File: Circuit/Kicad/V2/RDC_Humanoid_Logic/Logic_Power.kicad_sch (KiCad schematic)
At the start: 5 parts

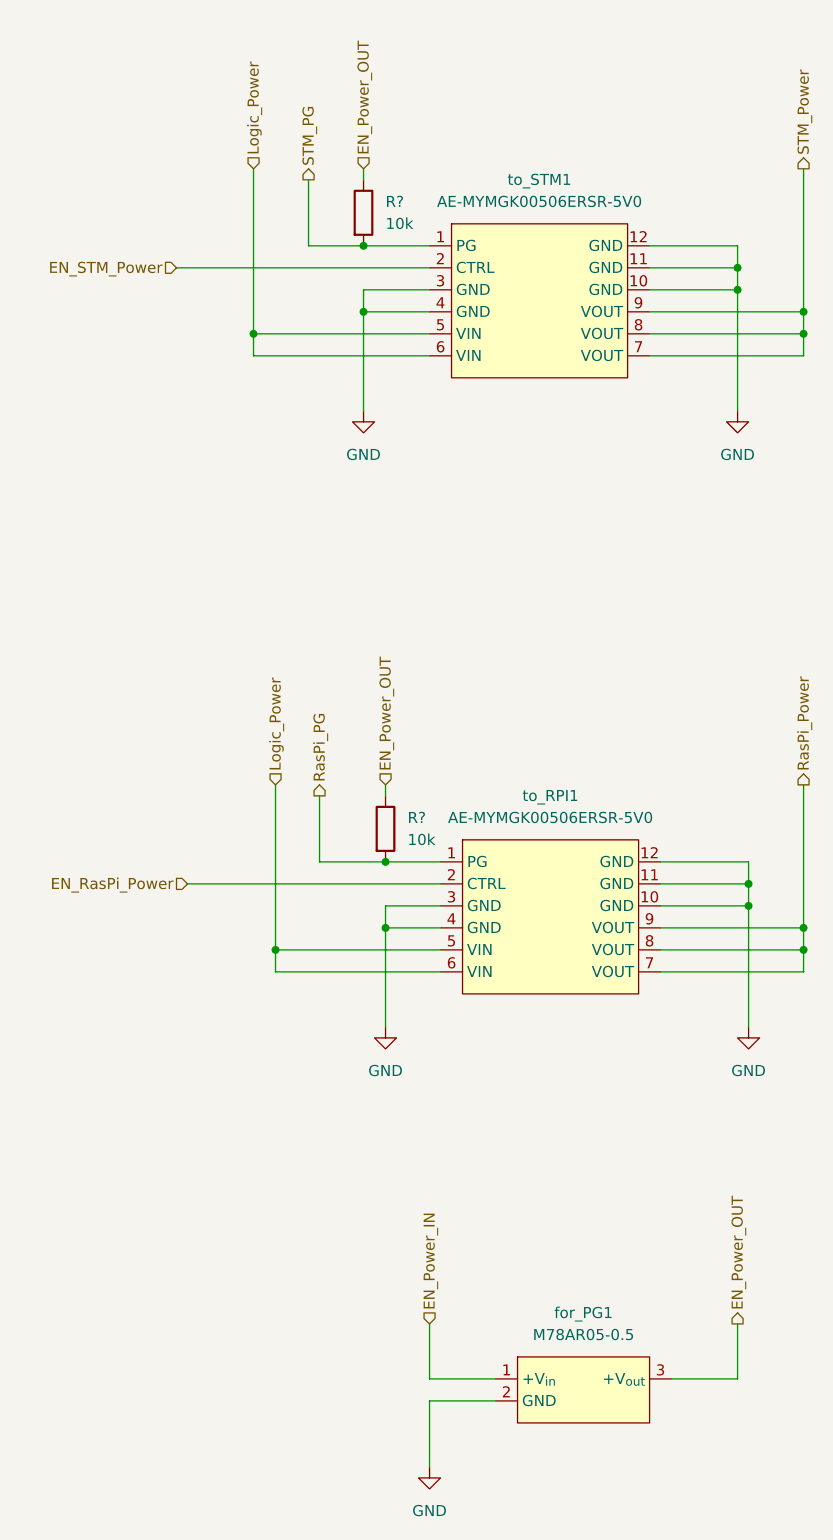
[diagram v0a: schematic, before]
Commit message: V2をUpdate。FrontをベタGND、CANトランシーバのSTANDBYとINをGNDに接続、ビアを複数配置、XT30->XT60に更新、D1を回路図通りショットキーバリアダイオードに変更した。
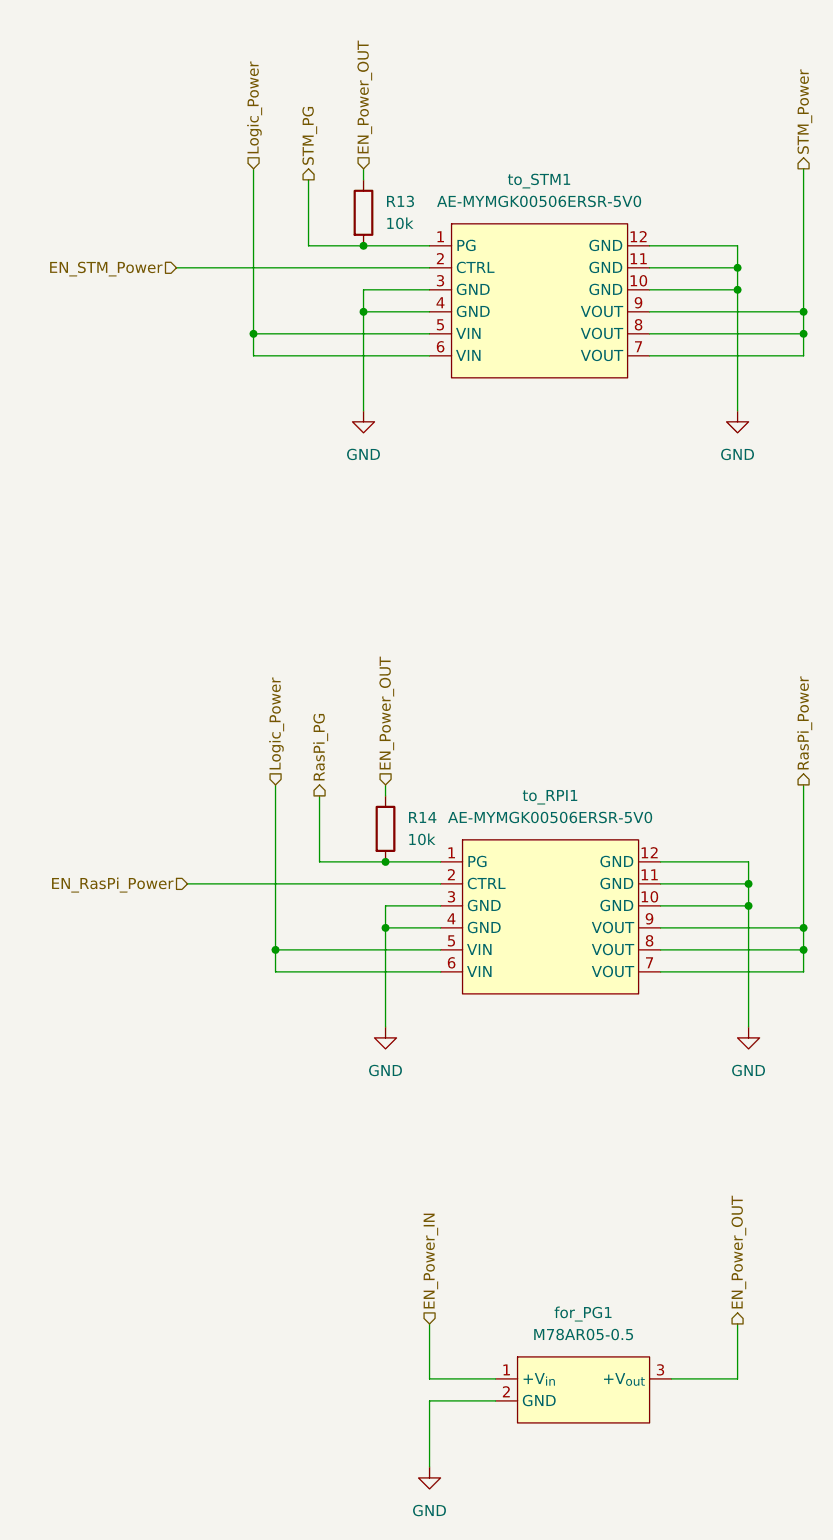
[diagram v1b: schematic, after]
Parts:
- gave numbers to parts that had none: 2
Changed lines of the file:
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@@
   (symbol (lib_id "power:GND") (at 111.76 133.35 0) (unit 1)
     (in_bom yes) (on_board yes) (dnp no) (fields_autoplaced)
-    (property "Reference" "#PWR04" (at 111.76 139.7 0)
+    (property "Reference" "#PWR034" (at 111.76 139.7 0)
       (effects (font (size 1.27 1.27)) hide)
     )
@@
     (instances
       (project "RDC_Humanoid_Logic"
-        (path "/2bec3ac6-4176-417a-a2e5-e81844f01e63"
-          (reference "#PWR04") (unit 1)
-        )
         (path "/2bec3ac6-4176-417a-a2e5-e81844f01e63/3cc3fb12-43c9-44a7-aafc-8cfc59ac2e26"
           (reference "#PWR034") (unit 1)
@@
     (instances
       (project "RDC_Humanoid_Logic"
-        (path "/2bec3ac6-4176-417a-a2e5-e81844f01e63"
-          (reference "to_RPI1") (unit 1)
-        )
         (path "/2bec3ac6-4176-417a-a2e5-e81844f01e63/3cc3fb12-43c9-44a7-aafc-8cfc59ac2e26"
           (reference "to_RPI1") (unit 1)
@@
     (instances
       (project "RDC_Humanoid_Logic"
-        (path "/2bec3ac6-4176-417a-a2e5-e81844f01e63"
+        (path "/2bec3ac6-4176-417a-a2e5-e81844f01e63/3cc3fb12-43c9-44a7-aafc-8cfc59ac2e26"
           (reference "to_STM1") (unit 1)
         )
-        (path "/2bec3ac6-4176-417a-a2e5-e81844f01e63/3cc3fb12-43c9-44a7-aafc-8cfc59ac2e26"
-          (reference "to_STM1") (unit 1)
-        )
       )
     )
@@
   (symbol (lib_id "power:GND") (at 109.22 62.23 0) (unit 1)
     (in_bom yes) (on_board yes) (dnp no) (fields_autoplaced)
-    (property "Reference" "#PWR05" (at 109.22 68.58 0)
+    (property "Reference" "#PWR033" (at 109.22 68.58 0)
       (effects (font (size 1.27 1.27)) hide)
     )
@@
     (instances
       (project "RDC_Humanoid_Logic"
-        (path "/2bec3ac6-4176-417a-a2e5-e81844f01e63"
-          (reference "#PWR05") (unit 1)
-        )
         (path "/2bec3ac6-4176-417a-a2e5-e81844f01e63/3cc3fb12-43c9-44a7-aafc-8cfc59ac2e26"
           (reference "#PWR033") (unit 1)
@@
   (symbol (lib_id "power:GND") (at 153.67 133.35 0) (unit 1)
     (in_bom yes) (on_board yes) (dnp no) (fields_autoplaced)
-    (property "Reference" "#PWR07" (at 153.67 139.7 0)
+    (property "Reference" "#PWR037" (at 153.67 139.7 0)
       (effects (font (size 1.27 1.27)) hide)
     )
@@
     (instances
       (project "RDC_Humanoid_Logic"
-        (path "/2bec3ac6-4176-417a-a2e5-e81844f01e63"
-          (reference "#PWR07") (unit 1)
-        )
         (path "/2bec3ac6-4176-417a-a2e5-e81844f01e63/3cc3fb12-43c9-44a7-aafc-8cfc59ac2e26"
           (reference "#PWR037") (unit 1)
@@
     (instances
       (project "RDC_Humanoid_Logic"
-        (path "/2bec3ac6-4176-417a-a2e5-e81844f01e63"
+        (path "/2bec3ac6-4176-417a-a2e5-e81844f01e63/3cc3fb12-43c9-44a7-aafc-8cfc59ac2e26"
           (reference "for_PG1") (unit 1)
         )
-        (path "/2bec3ac6-4176-417a-a2e5-e81844f01e63/3cc3fb12-43c9-44a7-aafc-8cfc59ac2e26"
-          (reference "for_PG1") (unit 1)
-        )
       )
     )
@@
   (symbol (lib_id "power:GND") (at 152.4 62.23 0) (unit 1)
     (in_bom yes) (on_board yes) (dnp no) (fields_autoplaced)
-    (property "Reference" "#PWR06" (at 152.4 68.58 0)
+    (property "Reference" "#PWR036" (at 152.4 68.58 0)
       (effects (font (size 1.27 1.27)) hide)
     )
@@
     (instances
       (project "RDC_Humanoid_Logic"
-        (path "/2bec3ac6-4176-417a-a2e5-e81844f01e63"
-          (reference "#PWR06") (unit 1)
-        )
         (path "/2bec3ac6-4176-417a-a2e5-e81844f01e63/3cc3fb12-43c9-44a7-aafc-8cfc59ac2e26"
           (reference "#PWR036") (unit 1)
@@
   (symbol (lib_id "Device:R") (at 109.22 39.37 0) (unit 1)
     (in_bom yes) (on_board yes) (dnp no) (fields_autoplaced)
-    (property "Reference" "R?" (at 111.76 38.1 0)
+    (property "Reference" "R13" (at 111.76 38.1 0)
       (effects (font (size 1.27 1.27)) (justify left))
     )
@@
     (instances
       (project "RDC_Humanoid_Logic"
-        (path "/2bec3ac6-4176-417a-a2e5-e81844f01e63"
-          (reference "R?") (unit 1)
-        )
         (path "/2bec3ac6-4176-417a-a2e5-e81844f01e63/3cc3fb12-43c9-44a7-aafc-8cfc59ac2e26"
           (reference "R13") (unit 1)
@@
   (symbol (lib_id "Device:R") (at 111.76 110.49 0) (unit 1)
     (in_bom yes) (on_board yes) (dnp no) (fields_autoplaced)
-    (property "Reference" "R?" (at 114.3 109.22 0)
+    (property "Reference" "R14" (at 114.3 109.22 0)
       (effects (font (size 1.27 1.27)) (justify left))
     )
@@
     (instances
       (project "RDC_Humanoid_Logic"
-        (path "/2bec3ac6-4176-417a-a2e5-e81844f01e63"
-          (reference "R?") (unit 1)
-        )
         (path "/2bec3ac6-4176-417a-a2e5-e81844f01e63/3cc3fb12-43c9-44a7-aafc-8cfc59ac2e26"
           (reference "R14") (unit 1)
@@
   (symbol (lib_id "power:GND") (at 116.84 184.15 0) (unit 1)
     (in_bom yes) (on_board yes) (dnp no) (fields_autoplaced)
-    (property "Reference" "#PWR09" (at 116.84 190.5 0)
+    (property "Reference" "#PWR035" (at 116.84 190.5 0)
       (effects (font (size 1.27 1.27)) hide)
     )
@@
     (instances
       (project "RDC_Humanoid_Logic"
-        (path "/2bec3ac6-4176-417a-a2e5-e81844f01e63"
-          (reference "#PWR09") (unit 1)
-        )
         (path "/2bec3ac6-4176-417a-a2e5-e81844f01e63/3cc3fb12-43c9-44a7-aafc-8cfc59ac2e26"
           (reference "#PWR035") (unit 1)
